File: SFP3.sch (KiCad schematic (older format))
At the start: 19 parts, among them J7 TYCO_1888247-1

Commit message: bugs fixed
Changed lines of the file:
@@
 $Descr A4 11693 8268
 encoding utf-8
-Sheet 11 25
+Sheet 10 25
 Title "Simple AFC"
 Date "2019-01-16"
@@
 Text Label 6550 1750 0    50   ~ 10
 SFP_3_TX_N
-Text HLabel 7400 1050 2    50   BiDi ~ 10
+Text HLabel 7400 1050 2    50   Output ~ 10
 SFP_3_RX_P
-Text HLabel 7400 1250 2    50   BiDi ~ 10
+Text HLabel 7400 1250 2    50   Output ~ 10
 SFP_3_RX_N
-Text HLabel 7400 1550 2    50   BiDi ~ 10
+Text HLabel 7400 1550 2    50   Input ~ 10
 SFP_3_TX_P
-Text HLabel 7400 1750 2    50   BiDi ~ 10
+Text HLabel 7400 1750 2    50   Input ~ 10
 SFP_3_TX_N
 Wire Wire Line

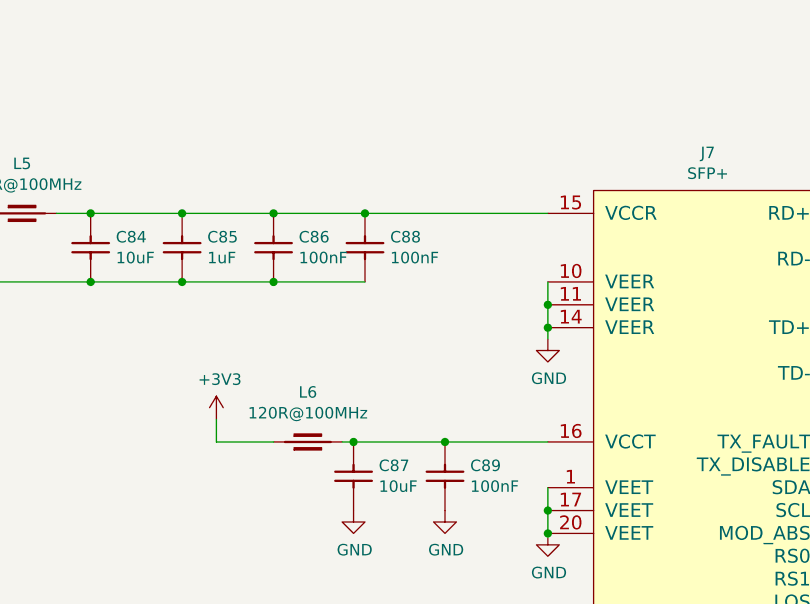
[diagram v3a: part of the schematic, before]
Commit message: SW2 placement changed, BOM cleared, FPGA boot, less ERC errors and wornings
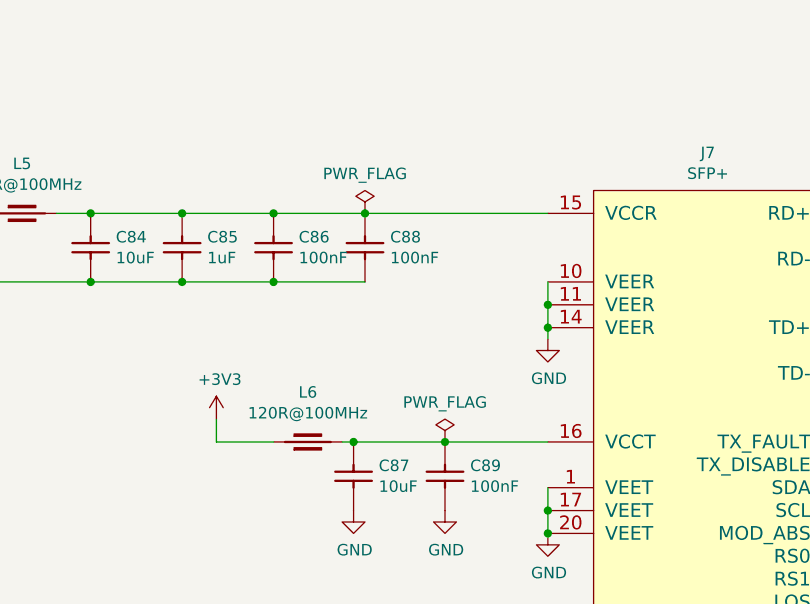
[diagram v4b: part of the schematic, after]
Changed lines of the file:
@@
 	6300 3550 6300 4000
 Connection ~ 4300 3350
+$Comp
+L power:PWR_FLAG #FLG?
+U 1 1 5D1E21F1
+P 3500 1950
+AR Path="/5BABAC65/5D1E21F1" Ref="#FLG?"  Part="1"
+AR Path="/5CC6DBF7/5D1E21F1" Ref="#FLG0108"  Part="1"
+F 0 "#FLG0108" H 3500 2025 50  0001 C CNN
+F 1 "PWR_FLAG" H 3500 2123 50  0000 C CNN
+F 2 "" H 3500 1950 50  0001 C CNN
+F 3 "~" H 3500 1950 50  0001 C CNN
+	1    3500 1950
+	1    0    0    -1
+$EndComp
+$Comp
+L power:PWR_FLAG #FLG?
+U 1 1 5D1E3C49
+P 3850 2950
+AR Path="/5BABAC65/5D1E3C49" Ref="#FLG?"  Part="1"
+AR Path="/5CC6DBF7/5D1E3C49" Ref="#FLG0109"  Part="1"
+F 0 "#FLG0109" H 3850 3025 50  0001 C CNN
+F 1 "PWR_FLAG" H 3850 3123 50  0000 C CNN
+F 2 "" H 3850 2950 50  0001 C CNN
+F 3 "~" H 3850 2950 50  0001 C CNN
+	1    3850 2950
+	1    0    0    -1
+$EndComp
 $EndSCHEMATC

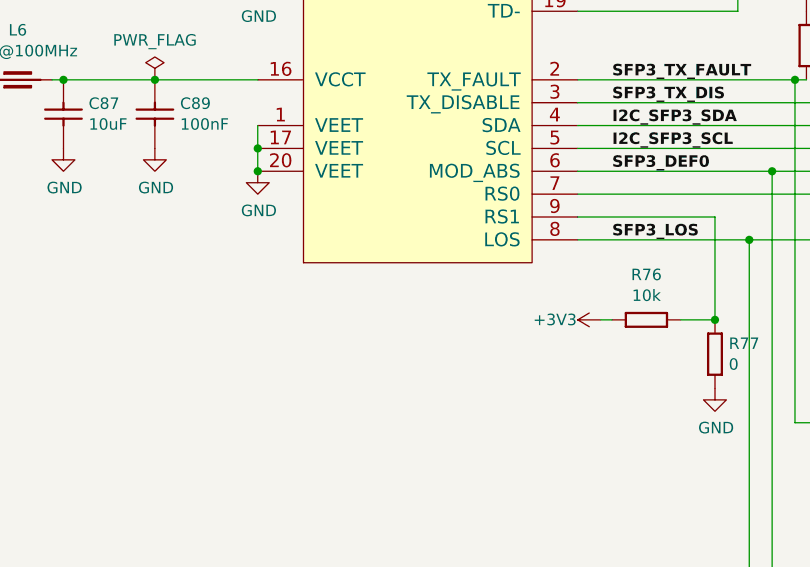
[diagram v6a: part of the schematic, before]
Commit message: SCH: shave down ERC to 1 error, 0 warning
  * 1 unavoidable error due to the unpopulated crystal Y2
  * change many pin types in symbol libraries (also for FMC con.)
  * as a result, could remove some power flags
  * fix footrint attribute for SFP module symbols

for most devices (not voltage regulators):
  * vcc = power input
  * gnd = power input
  * gpios (also FMC lanes) = bidirectional
  * configuration pins (tied to vcc / gnd) = inputs
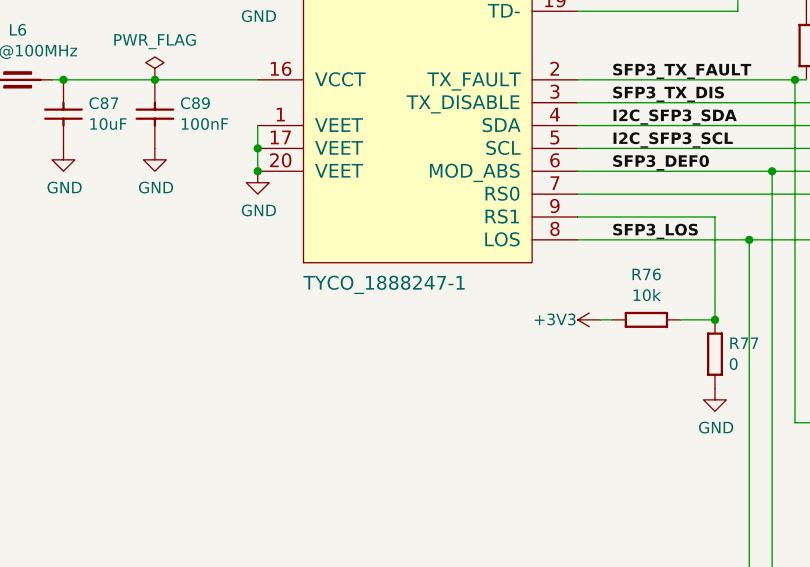
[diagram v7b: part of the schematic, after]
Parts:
- J7: footprint 1888247-1:TE_1888247-1 -> Marble:TE_1888247-1; Case ~~ -> (none); Comment ~~ -> (none); ComponentLink1Description ~~ -> (none); ComponentLink2Description ~~ -> (none); Database Table Name (none) -> TYCO; Device ~~ -> (none); Footprint Library (none) -> TYCO SMD; Library Name TYCO SMD -> Connectors.DbLib; PackageDescription ~~ -> (none); SCEM ~~ -> (none); Sense Comment ~~ -> (none); Status Comment ~~ -> (none)
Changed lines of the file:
@@
 $Descr A4 11693 8268
 encoding utf-8
-Sheet 10 25
+Sheet 9 25
 Title "Marble"
 Date "2019-01-16"
@@
 AR Path="/5CC6DBF7/5C8B7FD0" Ref="J7"  Part="1"
 F 0 "J7" H 5000 2015 50  0000 C CNN
-F 1 "TYCO_1888247-1" H 4500 -140 60  0001 L CNN
-F 2 "1888247-1:TE_1888247-1" H 4500 -950 60  0001 L CNN
+F 1 "TYCO_1888247-1" H 4500 -140 60  0000 L CNN
+F 2 "Marble:TE_1888247-1" H 4500 -950 60  0001 L CNN
 F 3 "" H 4500 -320 60  0001 L CNN
 F 4 "SFP+" H 5000 1924 50  0000 C CNN "~"
@@
 F 6 "SFP+x1" H 4500 -500 60  0001 L CNN "Library Ref"
 F 7 "SchLib\\Connectors.SchLib" H 4500 -590 60  0001 L CNN "Library Path"
-F 8 "~~" H 4500 -680 60  0001 L CNN "Comment"
+F 8 " " H 4500 -680 60  0001 L CNN "Comment"
 F 9 "Standard" H 4500 -770 60  0001 L CNN "Component Kind"
 F 10 "Standard" H 4500 -860 60  0001 L CNN "Component Type"
-F 11 "~~" H 4500 -1040 60  0001 L CNN "PackageDescription"
+F 11 " " H 4500 -1040 60  0001 L CNN "PackageDescription"
 F 12 "20" H 4500 -1130 60  0001 L CNN "Pin Count"
-F 13 "~~" H 4500 -1220 60  0001 L CNN "Case"
+F 13 " " H 4500 -1220 60  0001 L CNN "Case"
 F 14 "PcbLib\\TYCO SMD.PcbLib" H 4500 -1310 60  0001 L CNN "Footprint Path"
 F 15 "TYCO_1888247-1" H 4500 -1400 60  0001 L CNN "Footprint Ref"
@@
 F 20 "No" H 4500 -1850 60  0001 L CNN "PressFit"
 F 21 "No" H 4500 -1940 60  0001 L CNN "Sense"
-F 22 "~~" H 4500 -2030 60  0001 L CNN "Sense Comment"
+F 22 " " H 4500 -2030 60  0001 L CNN "Sense Comment"
 F 23 "None" H 4500 -2120 60  0001 L CNN "Status"
-F 24 "~~" H 4500 -2210 60  0001 L CNN "Status Comment"
-F 25 "~~" H 4500 -2300 60  0001 L CNN "SCEM"
-F 26 "~~" H 4500 -2390 60  0001 L CNN "Device"
+F 24 " " H 4500 -2210 60  0001 L CNN "Status Comment"
+F 25 " " H 4500 -2300 60  0001 L CNN "SCEM"
+F 26 " " H 4500 -2390 60  0001 L CNN "Device"
 F 27 "20 Position, Pitch 0.8mm SFP+ Receptacle (Small Form-factor Pluggable)" H 4500 -2480 60  0001 L CNN "Part Description"
 F 28 "TYCO ELECTRONICS" H 4500 -2570 60  0001 L CNN "Manufacturer"
@@
 F 30 "5.4mm" H 4500 -2750 60  0001 L CNN "ComponentHeight"
 F 31 "~~" H 4500 -2840 60  0001 L CNN "ComponentLink1URL"
-F 32 "~~" H 4500 -2930 60  0001 L CNN "ComponentLink1Description"
+F 32 " " H 4500 -2930 60  0001 L CNN "ComponentLink1Description"
 F 33 "~~" H 4500 -3020 60  0001 L CNN "ComponentLink2URL"
-F 34 "~~" H 4500 -3110 60  0001 L CNN "ComponentLink2Description"
+F 34 " " H 4500 -3110 60  0001 L CNN "ComponentLink2Description"
 F 35 "\\\\cern.ch\\dfs\\Applications\\Altium\\Datasheets\\TYCO_1888247-1.pdf" H 4500 -3200 60  0001 L CNN "HelpURL"
 F 36 "CERN DEM JLC" H 4500 -3290 60  0001 L CNN "Author"
 F 37 "02/27/12 00:00:00" H 4500 -3380 60  0001 L CNN "CreateDate"
 F 38 "02/27/12 00:00:00" H 4500 -3470 60  0001 L CNN "LatestRevisionDate"
-F 39 "TYCO SMD" H 4500 -3560 60  0001 L CNN "Library Name"
+F 39 "Connectors.DbLib" H 4500 -3560 60  0001 L CNN "Library Name"
 F 40 "This work is licensed under the Creative Commons CC-BY-SA 4.0 License. To the extent that circuit schematics that use Licensed Material can be considered to be ‘Adapted Material’, then the copyright holder waives article 3.b of the license with respect to these schematics." H 4500 -3650 60  0001 L CNN "License"
+F 41 "TYCO" H 4500 1850 50  0001 C CNN "Database Table Name"
+F 42 "TYCO SMD" H 4500 1850 50  0001 C CNN "Footprint Library"
 	1    4500 1850
 	1    0    0    -1

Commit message: Convert all footprints to use Marble nickname
Includes both .sch and .lib files
Includes both bare footprint names and those with CERN-like nicknames
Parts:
- C82, C86, C88, C89: footprint CAPC0603X33N -> Marble:CAPC0603X33N
- C83, C85: footprint CAPC1005X55N -> Marble:CAPC1005X55N
- C84, C87: footprint CAPC1608X87N -> Marble:CAPC1608X87N
- L5, L6: footprint INDC1608X65N -> Marble:INDC1608X65N
- R76, R77, R78, R79, R80, R81, R82, R84: footprint RESC1005X40N -> Marble:RESC1005X40N
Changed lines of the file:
@@
 F 0 "R78" V 6804 2710 50  0000 L CNN
 F 1 "R0402_10K_1%_0.0625W_100PPM" H 6700 2440 60  0001 L CNN
-F 2 "RESC1005X40N" H 6700 1630 60  0001 L CNN
+F 2 "Marble:RESC1005X40N" H 6700 1630 60  0001 L CNN
 F 3 "\\\\cern.ch\\dfs\\Applications\\Altium\\Datasheets\\R0402_Phycomp_RC0402.pdf" H 6700 2260 60  0001 L CNN
 F 4 "10k" V 6895 2710 50  0000 L CNN "~"
@@
 F 0 "R79" V 7054 2710 50  0000 L CNN
 F 1 "R0402_10K_1%_0.0625W_100PPM" H 6950 2440 60  0001 L CNN
-F 2 "RESC1005X40N" H 6950 1630 60  0001 L CNN
+F 2 "Marble:RESC1005X40N" H 6950 1630 60  0001 L CNN
 F 3 "\\\\cern.ch\\dfs\\Applications\\Altium\\Datasheets\\R0402_Phycomp_RC0402.pdf" H 6950 2260 60  0001 L CNN
 F 4 "10k" V 7145 2710 50  0000 L CNN "~"
@@
 F 0 "R80" V 7304 2710 50  0000 L CNN
 F 1 "R0402_10K_1%_0.0625W_100PPM" H 7200 2440 60  0001 L CNN
-F 2 "RESC1005X40N" H 7200 1630 60  0001 L CNN
+F 2 "Marble:RESC1005X40N" H 7200 1630 60  0001 L CNN
 F 3 "\\\\cern.ch\\dfs\\Applications\\Altium\\Datasheets\\R0402_Phycomp_RC0402.pdf" H 7200 2260 60  0001 L CNN
 F 4 "10k" V 7395 2710 50  0000 L CNN "~"
@@
 F 0 "R81" V 7554 2710 50  0000 L CNN
 F 1 "R0402_10K_1%_0.0625W_100PPM" H 7450 2440 60  0001 L CNN
-F 2 "RESC1005X40N" H 7450 1630 60  0001 L CNN
+F 2 "Marble:RESC1005X40N" H 7450 1630 60  0001 L CNN
 F 3 "\\\\cern.ch\\dfs\\Applications\\Altium\\Datasheets\\R0402_Phycomp_RC0402.pdf" H 7450 2260 60  0001 L CNN
 F 4 "10k" V 7645 2710 50  0000 L CNN "~"
@@
 F 0 "R82" V 7804 2710 50  0000 L CNN
 F 1 "R0402_10K_1%_0.0625W_100PPM" H 7700 2440 60  0001 L CNN
-F 2 "RESC1005X40N" H 7700 1630 60  0001 L CNN
+F 2 "Marble:RESC1005X40N" H 7700 1630 60  0001 L CNN
 F 3 "\\\\cern.ch\\dfs\\Applications\\Altium\\Datasheets\\R0402_Phycomp_RC0402.pdf" H 7700 2260 60  0001 L CNN
 F 4 "10k" V 7895 2710 50  0000 L CNN "~"
@@
 F 0 "C82" V 1254 2060 50  0000 L CNN
 F 1 "CC0201_100NF_6.3V_10%_X5R" H 1150 1690 60  0001 L CNN
-F 2 "CAPC0603X33N" H 1150 880 60  0001 L CNN
+F 2 "Marble:CAPC0603X33N" H 1150 880 60  0001 L CNN
 F 3 "\\\\cern.ch\\dfs\\Applications\\Altium\\Datasheets\\CC0201_X5R_AVX.pdf" H 1150 1510 60  0001 L CNN
 F 4 "100nF" V 1345 2060 50  0000 L CNN "~"
@@
 F 0 "C86" V 3204 2060 50  0000 L CNN
 F 1 "CC0201_100NF_6.3V_10%_X5R" H 3100 1690 60  0001 L CNN
-F 2 "CAPC0603X33N" H 3100 880 60  0001 L CNN
+F 2 "Marble:CAPC0603X33N" H 3100 880 60  0001 L CNN
 F 3 "\\\\cern.ch\\dfs\\Applications\\Altium\\Datasheets\\CC0201_X5R_AVX.pdf" H 3100 1510 60  0001 L CNN
 F 4 "100nF" V 3295 2060 50  0000 L CNN "~"
@@
 F 0 "C88" V 3604 2060 50  0000 L CNN
 F 1 "CC0201_100NF_6.3V_10%_X5R" H 3500 1690 60  0001 L CNN
-F 2 "CAPC0603X33N" H 3500 880 60  0001 L CNN
+F 2 "Marble:CAPC0603X33N" H 3500 880 60  0001 L CNN
 F 3 "\\\\cern.ch\\dfs\\Applications\\Altium\\Datasheets\\CC0201_X5R_AVX.pdf" H 3500 1510 60  0001 L CNN
 F 4 "100nF" V 3695 2060 50  0000 L CNN "~"
@@
 F 0 "C89" V 3954 3060 50  0000 L CNN
 F 1 "CC0201_100NF_6.3V_10%_X5R" H 3850 2690 60  0001 L CNN
-F 2 "CAPC0603X33N" H 3850 1880 60  0001 L CNN
+F 2 "Marble:CAPC0603X33N" H 3850 1880 60  0001 L CNN
 F 3 "\\\\cern.ch\\dfs\\Applications\\Altium\\Datasheets\\CC0201_X5R_AVX.pdf" H 3850 2510 60  0001 L CNN
 F 4 "100nF" V 4045 3060 50  0000 L CNN "~"
@@
 F 0 "L5" H 2000 2167 50  0000 C CNN
 F 1 "IND0603_MURATA_BLM18SG121TN1D" H 1850 1760 60  0001 L CNN
-F 2 "INDC1608X65N" H 1850 950 60  0001 L CNN
+F 2 "Marble:INDC1608X65N" H 1850 950 60  0001 L CNN
 F 3 "\\\\cern.ch\\dfs\\Applications\\Altium\\Datasheets\\IND0603_MURATA_BLM18S.pdf" H 1850 1580 60  0001 L CNN
 F 4 "120R@100MHz" H 2000 2076 50  0000 C CNN "~"
@@
 F 0 "L6" H 3250 3167 50  0000 C CNN
 F 1 "IND0603_MURATA_BLM18SG121TN1D" H 3100 2760 60  0001 L CNN
-F 2 "INDC1608X65N" H 3100 1950 60  0001 L CNN
+F 2 "Marble:INDC1608X65N" H 3100 1950 60  0001 L CNN
 F 3 "\\\\cern.ch\\dfs\\Applications\\Altium\\Datasheets\\IND0603_MURATA_BLM18S.pdf" H 3100 2580 60  0001 L CNN
 F 4 "120R@100MHz" H 3250 3076 50  0000 C CNN "~"
@@
 F 0 "R76" H 6300 3803 50  0000 C CNN
 F 1 "R0402_10K_1%_0.0625W_100PPM" H 6150 3790 60  0001 L CNN
-F 2 "RESC1005X40N" H 6150 2980 60  0001 L CNN
+F 2 "Marble:RESC1005X40N" H 6150 2980 60  0001 L CNN
 F 3 "\\\\cern.ch\\dfs\\Applications\\Altium\\Datasheets\\R0402_Phycomp_RC0402.pdf" H 6150 3610 60  0001 L CNN
 F 4 "10k" H 6300 3894 50  0000 C CNN "~"
@@
 F 0 "R77" V 6404 4060 50  0000 L CNN
 F 1 "R0402_0R_JUMPER" H 6300 3790 60  0001 L CNN
-F 2 "RESC1005X40N" H 6300 2980 60  0001 L CNN
+F 2 "Marble:RESC1005X40N" H 6300 2980 60  0001 L CNN
 F 3 "\\\\cern.ch\\dfs\\Applications\\Altium\\Datasheets\\R0402_Phycomp_RC0402.pdf" H 6300 3610 60  0001 L CNN
 F 4 "0" V 6495 4060 50  0000 L CNN "~"
@@
 F 0 "C83" V 1704 2060 50  0000 L CNN
 F 1 "CC0402_1UF_16V_10%_X5R" H 1600 1690 60  0001 L CNN
-F 2 "CAPC1005X55N" H 1600 880 60  0001 L CNN
+F 2 "Marble:CAPC1005X55N" H 1600 880 60  0001 L CNN
 F 3 "\\\\cern.ch\\dfs\\Applications\\Altium\\Datasheets\\CC0402_X5R_TDK_C.pdf" H 1600 1510 60  0001 L CNN
 F 4 "1uF" V 1795 2060 50  0000 L CNN "~"
@@
 F 0 "C85" V 2804 2060 50  0000 L CNN
 F 1 "CC0402_1UF_16V_10%_X5R" H 2700 1690 60  0001 L CNN
-F 2 "CAPC1005X55N" H 2700 880 60  0001 L CNN
+F 2 "Marble:CAPC1005X55N" H 2700 880 60  0001 L CNN
 F 3 "\\\\cern.ch\\dfs\\Applications\\Altium\\Datasheets\\CC0402_X5R_TDK_C.pdf" H 2700 1510 60  0001 L CNN
 F 4 "1uF" V 2895 2060 50  0000 L CNN "~"
@@
 F 0 "C84" V 2496 2140 50  0000 R CNN
 F 1 "CC0603_10UF_6.3V_20%_X5R" H 2300 1990 60  0001 L CNN
-F 2 "CAPC1608X87N" H 2300 1180 60  0001 L CNN
+F 2 "Marble:CAPC1608X87N" H 2300 1180 60  0001 L CNN
 F 3 "\\\\cern.ch\\dfs\\Applications\\Altium\\Datasheets\\CC0603_X5R_KEMET.pdf" H 2300 1810 60  0001 L CNN
 F 4 "10uF" V 2405 2140 50  0000 R CNN "~"
@@
 F 0 "C87" V 3646 3140 50  0000 R CNN
 F 1 "CC0603_10UF_6.3V_20%_X5R" H 3450 2990 60  0001 L CNN
-F 2 "CAPC1608X87N" H 3450 2180 60  0001 L CNN
+F 2 "Marble:CAPC1608X87N" H 3450 2180 60  0001 L CNN
 F 3 "\\\\cern.ch\\dfs\\Applications\\Altium\\Datasheets\\CC0603_X5R_KEMET.pdf" H 3450 2810 60  0001 L CNN
 F 4 "10uF" V 3555 3140 50  0000 R CNN "~"
@@
 F 0 "R84" V 7854 3910 50  0000 L CNN
 F 1 "R0402_10K_1%_0.0625W_100PPM" H 7750 3640 60  0001 L CNN
-F 2 "RESC1005X40N" H 7750 2830 60  0001 L CNN
+F 2 "Marble:RESC1005X40N" H 7750 2830 60  0001 L CNN
 F 3 "\\\\cern.ch\\dfs\\Applications\\Altium\\Datasheets\\R0402_Phycomp_RC0402.pdf" H 7750 3460 60  0001 L CNN
 F 4 "10k" V 7945 3910 50  0000 L CNN "~"
